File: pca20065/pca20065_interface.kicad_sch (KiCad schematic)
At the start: 48 parts, among them J4 SF72S006VBxR2500, J6 ${ALTIUM_VALUE}, P1 ${ALTIUM_VALUE}, P8 ${ALTIUM_VALUE}, P9 ${ALTIUM_VALUE}, Q6 ${ALTIUM_VALUE}, SW2 ${ALTIUM_VALUE}, SW3 ${ALTIUM_VALUE}, SW4 ${ALTIUM_VALUE}, U1 ${ALTIUM_VALUE}, U15 MFFx_M2M_UICC, U24 ${ALTIUM_VALUE}, U8 ${ALTIUM_VALUE}

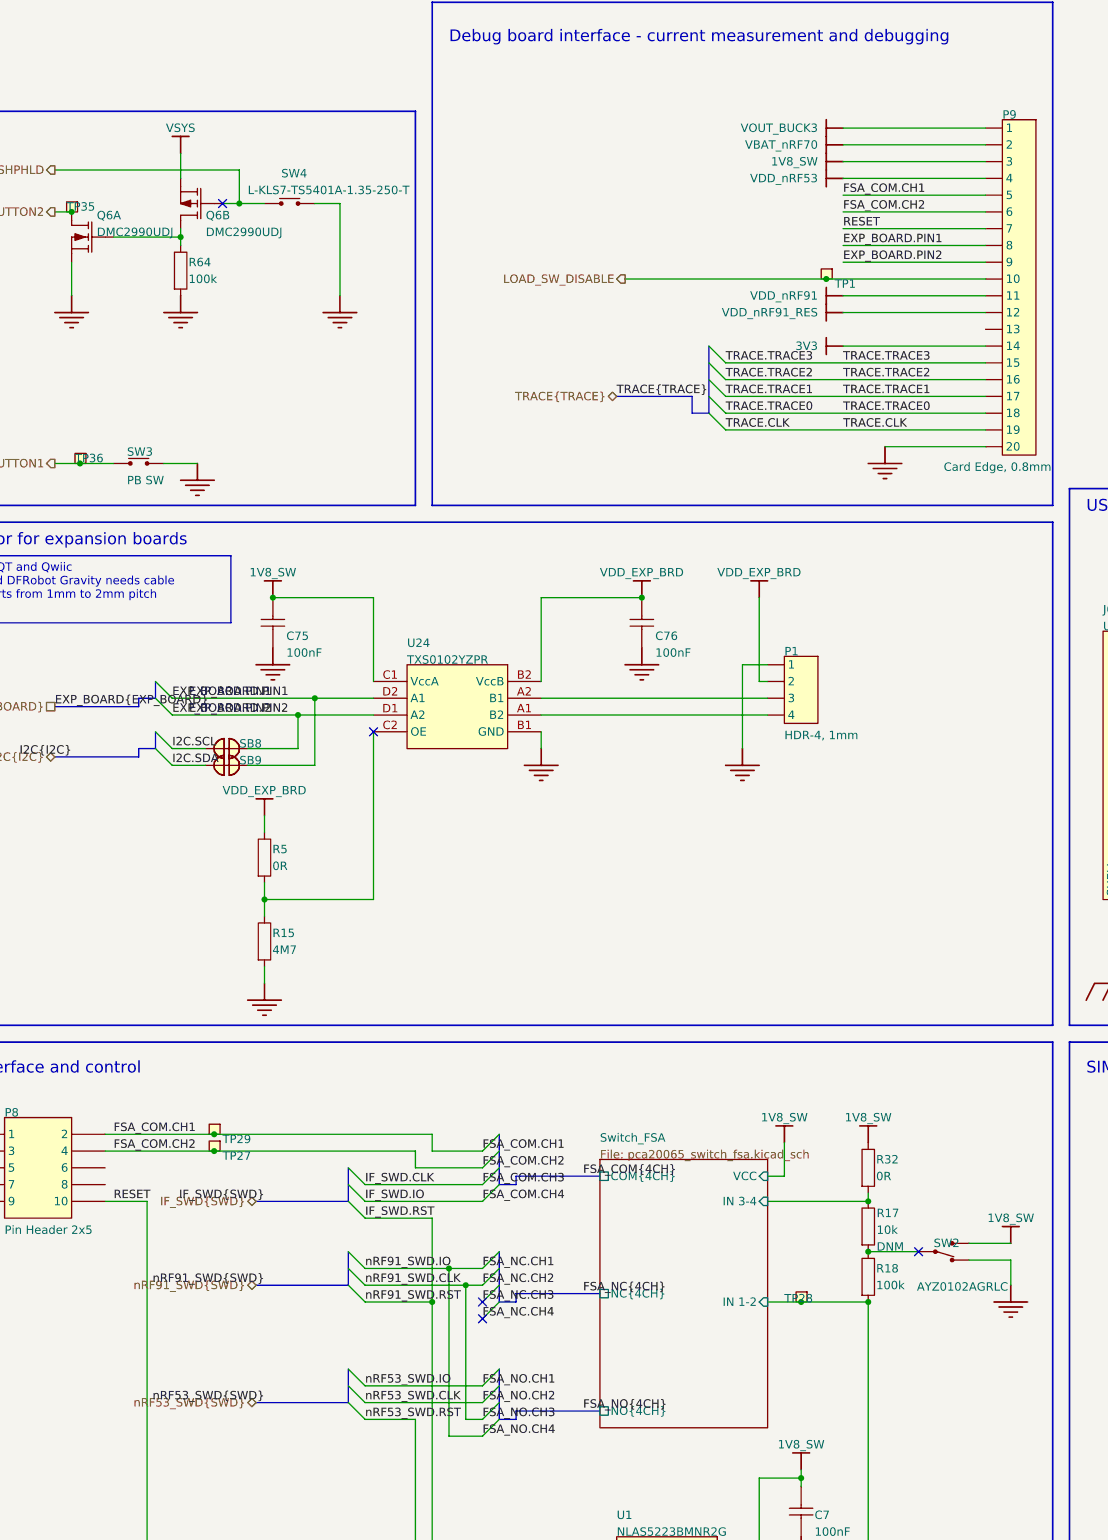
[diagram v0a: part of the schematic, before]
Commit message: Replaced nrf5340 with nrf54l15
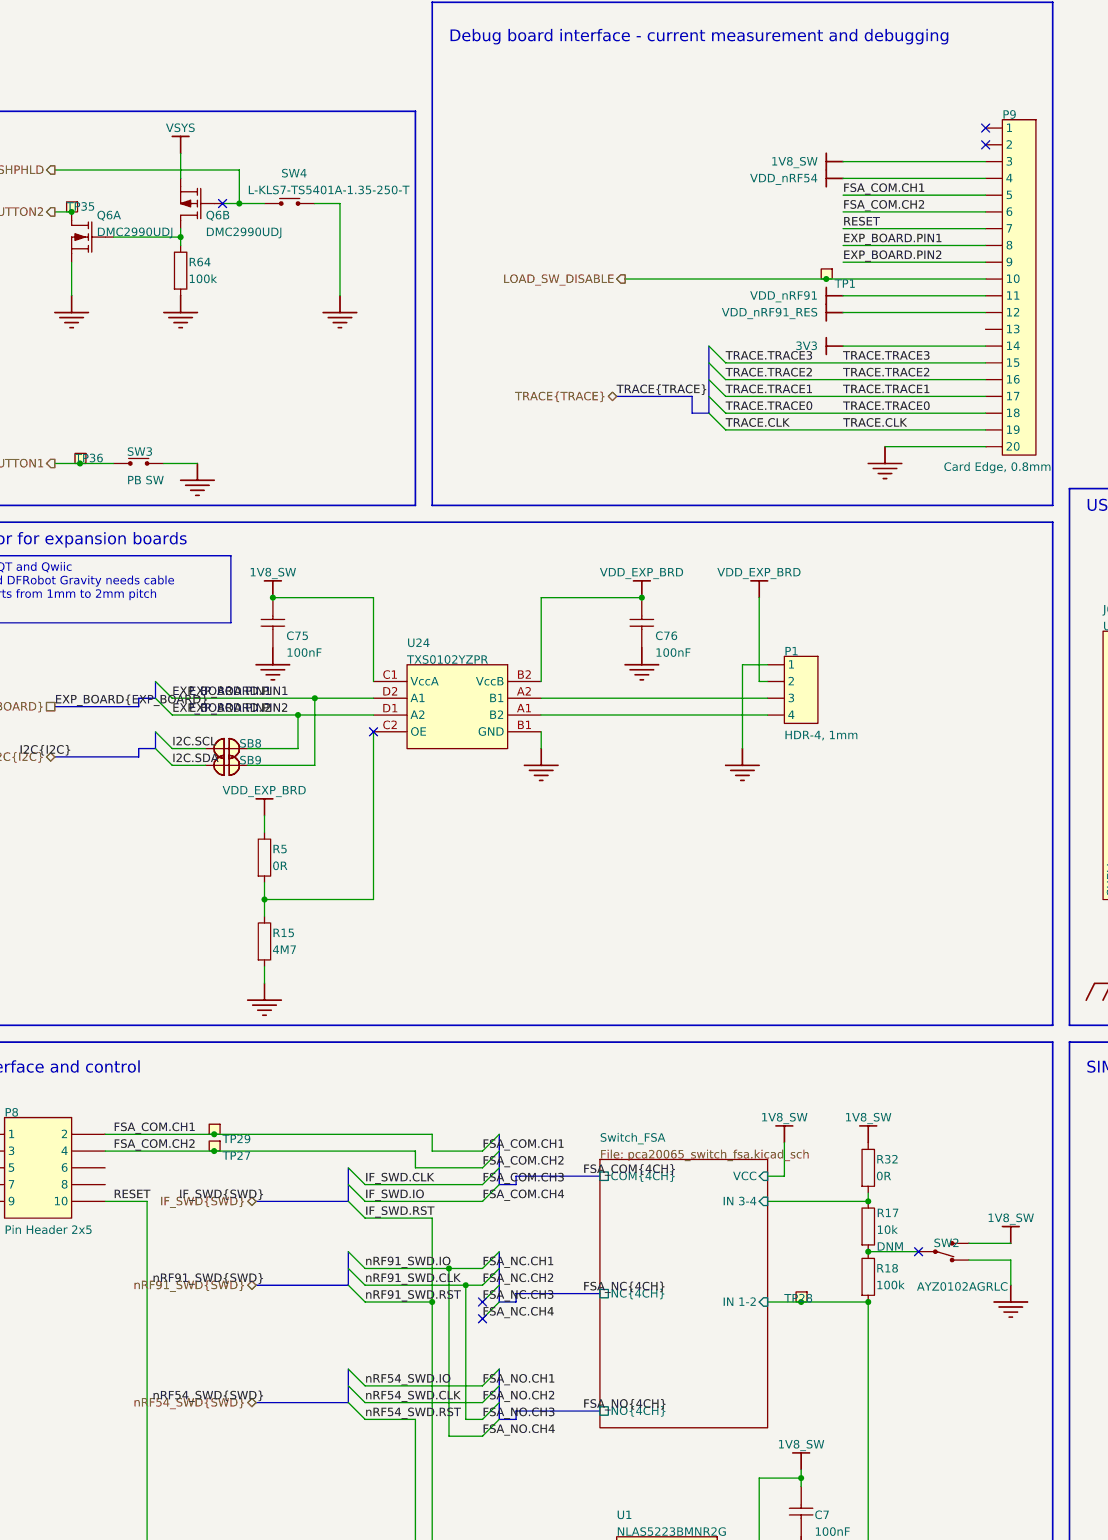
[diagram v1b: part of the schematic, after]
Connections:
- net VBAT_nRF70: no longer names the net of P9.2
- net VDD_nRF53 renamed VDD_nRF54
- net VOUT_BUCK3: no longer names the net of P9.1
- net nRF53_SWD.RST renamed nRF54_SWD.RST
- no-connect marks 12 -> 14
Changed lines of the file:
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@@
 		)
 	)
-	(wire
-		(pts
-			(xy 148.59 43.0022) (xy 170.18 43.0022)
-		)
-		(stroke
-			(width 0)
-			(type default)
-		)
-	)
 	(bus
 		(pts
@@
 	(wire
 		(pts
-			(xy 148.59 40.4622) (xy 170.18 40.4622)
-		)
-		(stroke
-			(width 0)
-			(type default)
-		)
-	)
-	(wire
-		(pts
 			(xy 148.59 68.4022) (xy 170.18 68.4022)
 		)
@@
 		)
 	)
-	(label "nRF53_SWD{SWD}"
+	(label "nRF54_SWD{SWD}"
 		(at 60.96 233.5022 180)
 		(effects
@@
 		)
 	)
-	(label "nRF53_SWD.CLK"
+	(label "nRF54_SWD.CLK"
 		(at 76.2 233.5022 0)
 		(effects
@@
 		)
 	)
-	(label "nRF53_SWD.RST"
+	(label "nRF54_SWD.RST"
 		(at 76.2 236.0422 0)
 		(effects
@@
 		)
 	)
-	(label "nRF53_SWD.IO"
+	(label "nRF54_SWD.IO"
 		(at 76.2 230.9622 0)
 		(effects
@@
 		)
 	)
-	(hierarchical_label "nRF53_SWD{SWD}"
+	(hierarchical_label "nRF54_SWD{SWD}"
 		(shape bidirectional)
 		(at 59.69 233.5022 180)
@@
 	)
 	(symbol
-		(lib_id "pca20065:VOUT_BUCK3_BAR")
-		(at 148.59 40.4622 270)
-		(unit 1)
-		(body_style 1)
-		(exclude_from_sim no)
-		(in_bom yes)
-		(on_board yes)
-		(in_pos_files yes)
-		(dnp no)
-		(property "Reference" "#PWR0253"
-			(at 148.59 40.4622 0)
-			(hide yes)
-			(show_name no)
-			(do_not_autoplace no)
-			(effects
-				(font
-					(size 1.27 1.27)
-				)
-			)
-		)
-		(property "Value" "VOUT_BUCK3"
-			(at 144.78 40.4622 90)
-			(show_name no)
-			(do_not_autoplace no)
-			(effects
-				(font
-					(size 1.27 1.27)
-				)
-				(justify right)
-			)
-		)
-		(property "Footprint" ""
-			(at 148.59 40.4622 0)
-			(show_name no)
-			(do_not_autoplace no)
-			(effects
-				(font
-					(size 1.27 1.27)
-				)
-			)
-		)
-		(property "Datasheet" ""
-			(at 148.59 40.4622 0)
-			(show_name no)
-			(do_not_autoplace no)
-			(effects
-				(font
-					(size 1.27 1.27)
-				)
-			)
-		)
-		(property "Description" ""
-			(at 148.59 40.4622 0)
-			(show_name no)
-			(do_not_autoplace no)
-			(effects
-				(font
-					(size 1.27 1.27)
-				)
-			)
-		)
-		(pin ""
-		)
-		(instances
-			(project "pca20065"
-				(path "/e5e493b2-5db2-4cc1-9a09-b26f233e4f86/d4ab6c1b-6878-4200-97f2-488e8c9baa6f"
-					(reference "#PWR0253")
-					(unit 1)
-				)
-			)
-		)
-	)
-	(symbol
 		(lib_name "CAP_7")
 		(lib_id "pca20065:CAP_7")
@@
 	)
 	(symbol
-		(lib_id "pca20065:VBAT_nRF70_BAR")
-		(at 148.59 43.0022 270)
-		(unit 1)
-		(body_style 1)
-		(exclude_from_sim no)
-		(in_bom yes)
-		(on_board yes)
-		(in_pos_files yes)
-		(dnp no)
-		(property "Reference" "#PWR0254"
-			(at 148.59 43.0022 0)
-			(hide yes)
-			(show_name no)
-			(do_not_autoplace no)
-			(effects
-				(font
-					(size 1.27 1.27)
-				)
-			)
-		)
-		(property "Value" "VBAT_nRF70"
-			(at 144.78 43.0022 90)
-			(show_name no)
-			(do_not_autoplace no)
-			(effects
-				(font
-					(size 1.27 1.27)
-				)
-				(justify right)
-			)
-		)
-		(property "Footprint" ""
-			(at 148.59 43.0022 0)
-			(show_name no)
-			(do_not_autoplace no)
-			(effects
-				(font
-					(size 1.27 1.27)
-				)
-			)
-		)
-		(property "Datasheet" ""
-			(at 148.59 43.0022 0)
-			(show_name no)
-			(do_not_autoplace no)
-			(effects
-				(font
-					(size 1.27 1.27)
-				)
-			)
-		)
-		(property "Description" ""
-			(at 148.59 43.0022 0)
-			(show_name no)
-			(do_not_autoplace no)
-			(effects
-				(font
-					(size 1.27 1.27)
-				)
-			)
-		)
-		(pin ""
-		)
-		(instances
-			(project "pca20065"
-				(path "/e5e493b2-5db2-4cc1-9a09-b26f233e4f86/d4ab6c1b-6878-4200-97f2-488e8c9baa6f"
-					(reference "#PWR0254")
-					(unit 1)
-				)
-			)
-		)
-	)
-	(symbol
 		(lib_id "pca20065:SF72S006VBxR2500")
 		(at 344.17 192.8622 0)
@@
 	)
 	(symbol
-		(lib_id "pca20065:VDD_nRF53_BAR")
+		(lib_id "pca20065:VDD_nRF54_BAR")
 		(at 148.59 48.0822 270)
 		(unit 1)
@@
 			)
 		)
-		(property "Value" "VDD_nRF53"
+		(property "Value" "VDD_nRF54"
 			(at 144.78 48.0822 90)
 			(show_name no)
@@
 			(project "pca20065"
 				(path "/e5e493b2-5db2-4cc1-9a09-b26f233e4f86/d4ab6c1b-6878-4200-97f2-488e8c9baa6f"
-					(page "9")
+					(page "8")
 				)
 			)
@@
 			(project "pca20065"
 				(path "/e5e493b2-5db2-4cc1-9a09-b26f233e4f86/d4ab6c1b-6878-4200-97f2-488e8c9baa6f"
-					(page "10")
+					(page "9")
 				)
 			)
 		)
 	)
+	(no_connect
+		(at 170.1800 40.4622)
+	)
+	(no_connect
+		(at 170.1800 43.0022)
+	)
 )

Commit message: Cleaned up
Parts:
- removed P8: ${ALTIUM_VALUE}, pca20065-import-fps:HDR_2x5-SMD-1.27mm-ANG, symbol pca20065:CONN-2x5
- removed P9: ${ALTIUM_VALUE}, pca20065-import-fps:10056847-101LF, symbol pca20065:CONN-20
- removed R17, R18: ${ALTIUM_VALUE}, pca20065-import-fps:RESC0603X03L_C, symbol pca20065:RES
- removed R32: ${ALTIUM_VALUE}, pca20065-import-fps:RESC0603X03L_C, symbol pca20065:RES_1
- removed SW2: ${ALTIUM_VALUE}, pca20065-import-fps:AYZ0102AGRLC, symbol pca20065:SW-SPDT
- removed TP27, TP28, TP29: ${ALTIUM_VALUE}, pca20065-import-fps:TP_SMD_D1.5mm, symbol pca20065:TESTPAD
- removed U1: ${ALTIUM_VALUE}, pca20065-import-fps:UFQFN40P140X180X55-10N, symbol pca20065:IC_SW_Dual_SPDT_10-pin_var1
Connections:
- no-connect marks 14 -> 7
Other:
- removed sheet Switch_FSA
- note added: "Load switch disable"
- note removed: "Debug board interface - current measurement and debugging"
